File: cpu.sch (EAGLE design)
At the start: 86 parts, among them X1 ED060SC4_EINK, X10 PIIKKIRIMA-4, X2 PIIKKIRIMA-5, X3 PIIKKIRIMA-2, X4 629105136821, X5 693071010811, X6 PIIKKIRIMA-6, X7 PIIKKIRIMA-2, X8 PIIKKIRIMA-2, X9 PIIKKIRIMA-2

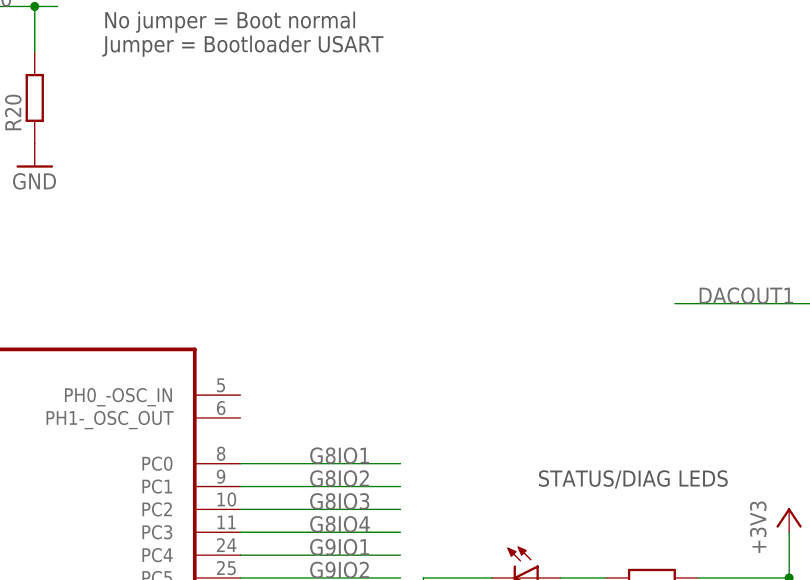
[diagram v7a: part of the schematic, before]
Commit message: HSE Crystal added
Added G1, 3.2x2.5 mm crystal. bottom.
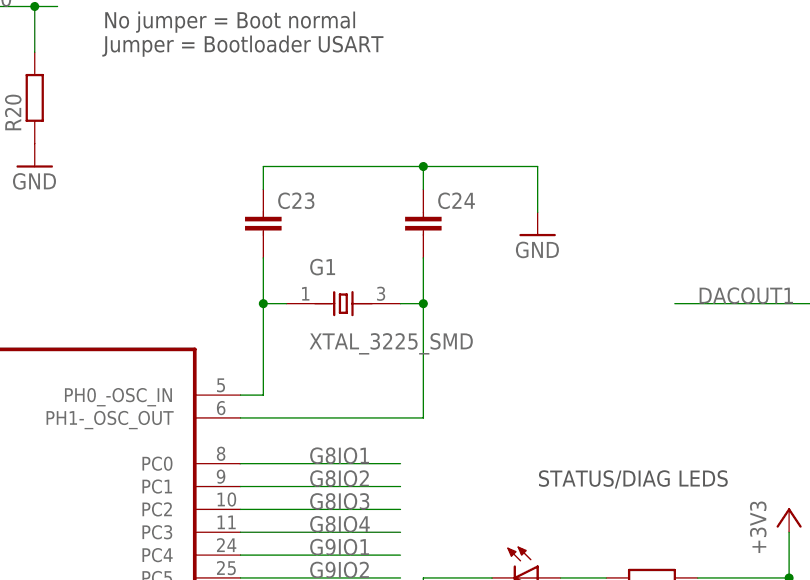
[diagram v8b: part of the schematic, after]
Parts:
- added C23, C24: (no value), rcl:C-EUC0603
- added G1: XTAL_3225_SMD, OMAT_IC:XTAL_3225_SMD
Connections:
- new net N$12: C23.2, D1.PH0_-OSC_IN, G1.X1
- new net N$14: C24.2, D1.PH1-_OSC_OUT, G1.X2
- net GND: now also C23.1, C24.1
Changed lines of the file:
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@@
 <part name="GND40" library="supply1" deviceset="GND" device=""/>
 <part name="+3V13" library="supply1" deviceset="+3V3" device=""/>
+<part name="G1" library="OMAT_IC" deviceset="XTAL_3225_SMD" device=""/>
+<part name="C23" library="rcl" deviceset="C-EU" device="C0603"/>
+<part name="C24" library="rcl" deviceset="C-EU" device="C0603"/>
+<part name="GND41" library="supply1" deviceset="GND" device=""/>
 </parts>
 <sheets>
@@
 <instance part="GND40" gate="1" x="325.12" y="152.4"/>
 <instance part="+3V13" gate="G$1" x="378.46" y="121.92"/>
+<instance part="G1" gate="G$1" x="177.8" y="210.82"/>
+<instance part="C23" gate="G$1" x="165.1" y="226.06"/>
+<instance part="C24" gate="G$1" x="182.88" y="226.06"/>
+<instance part="GND41" gate="1" x="195.58" y="223.52"/>
 </instances>
 <busses>
@@
 <wire x1="325.12" y1="157.48" x2="325.12" y2="154.94" width="0.1524" layer="91"/>
 <junction x="325.12" y="157.48"/>
+</segment>
+<segment>
+<pinref part="C23" gate="G$1" pin="1"/>
+<wire x1="165.1" y1="228.6" x2="165.1" y2="231.14" width="0.1524" layer="91"/>
+<wire x1="165.1" y1="231.14" x2="182.88" y2="231.14" width="0.1524" layer="91"/>
+<wire x1="182.88" y1="231.14" x2="195.58" y2="231.14" width="0.1524" layer="91"/>
+<wire x1="195.58" y1="231.14" x2="195.58" y2="226.06" width="0.1524" layer="91"/>
+<pinref part="GND41" gate="1" pin="GND"/>
+<pinref part="C24" gate="G$1" pin="1"/>
+<wire x1="182.88" y1="228.6" x2="182.88" y2="231.14" width="0.1524" layer="91"/>
+<junction x="182.88" y="231.14"/>
 </segment>
 </net>
@@
 </segment>
 </net>
+<net name="N$12" class="0">
+<segment>
+<pinref part="D1" gate="A" pin="PH0_-OSC_IN"/>
+<wire x1="162.56" y1="205.74" x2="165.1" y2="205.74" width="0.1524" layer="91"/>
+<wire x1="165.1" y1="205.74" x2="165.1" y2="215.9" width="0.1524" layer="91"/>
+<pinref part="G1" gate="G$1" pin="X1"/>
+<wire x1="165.1" y1="215.9" x2="167.64" y2="215.9" width="0.1524" layer="91"/>
+<pinref part="C23" gate="G$1" pin="2"/>
+<wire x1="165.1" y1="220.98" x2="165.1" y2="215.9" width="0.1524" layer="91"/>
+<junction x="165.1" y="215.9"/>
+</segment>
+</net>
+<net name="N$14" class="0">
+<segment>
+<pinref part="D1" gate="A" pin="PH1-_OSC_OUT"/>
+<wire x1="162.56" y1="203.2" x2="182.88" y2="203.2" width="0.1524" layer="91"/>
+<wire x1="182.88" y1="203.2" x2="182.88" y2="215.9" width="0.1524" layer="91"/>
+<pinref part="G1" gate="G$1" pin="X2"/>
+<wire x1="182.88" y1="215.9" x2="180.34" y2="215.9" width="0.1524" layer="91"/>
+<pinref part="C24" gate="G$1" pin="2"/>
+<wire x1="182.88" y1="220.98" x2="182.88" y2="215.9" width="0.1524" layer="91"/>
+<junction x="182.88" y="215.9"/>
+</segment>
+</net>
